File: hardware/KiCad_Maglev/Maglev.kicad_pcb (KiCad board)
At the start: 4 copper layers, 265 x 130 mm, 97 parts, among them IC1 TLV1117LV33DCYR, J1 USB_C_Receptacle, J2 691103110002, J3 61300621121, J4 61300821121, J5 61300821121, J6 61300621121, U1 WE-TVS-82400102, U2 ESP32-C3, U4 TMAG5173A2QDBVRQ1, U5 TPS259474ARPWR, Y1 IQXC-42_830108213209

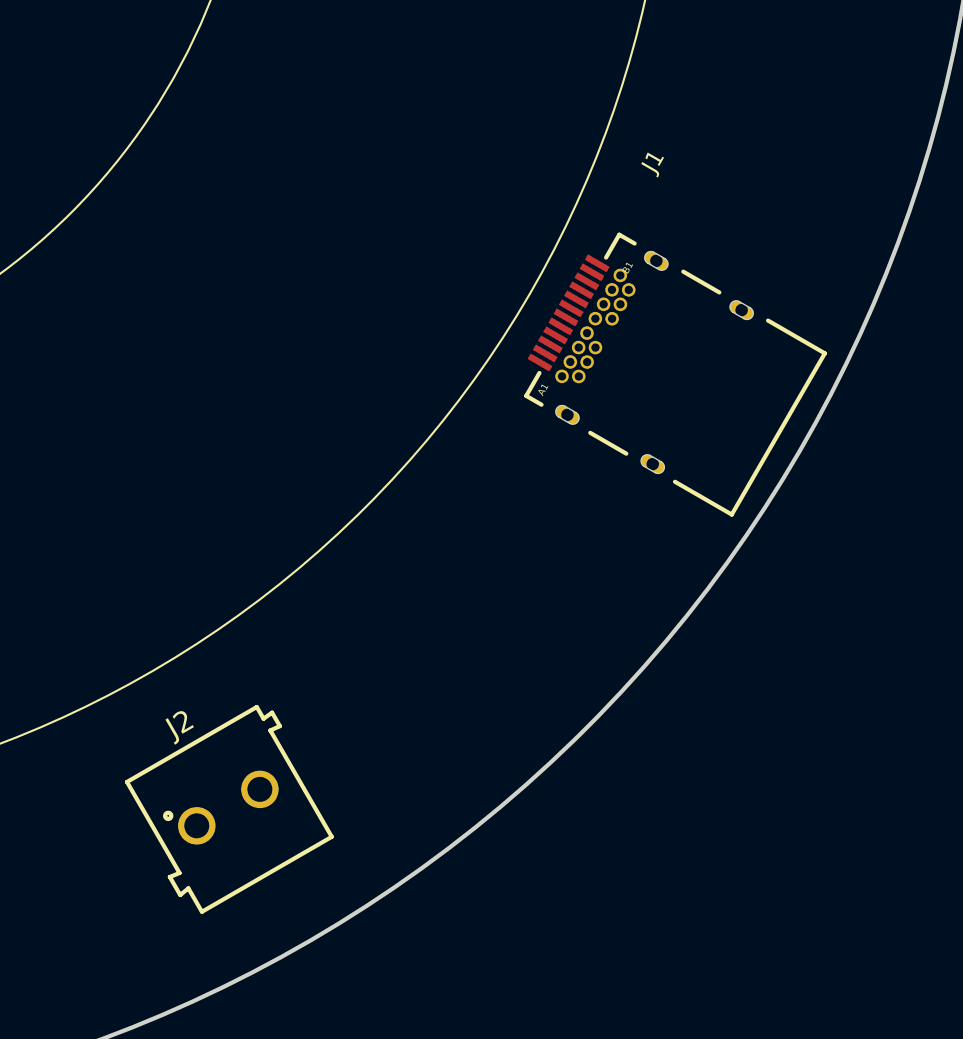
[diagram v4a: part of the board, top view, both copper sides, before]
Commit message: changed usb connector from 30deg to 45deg for easier routing
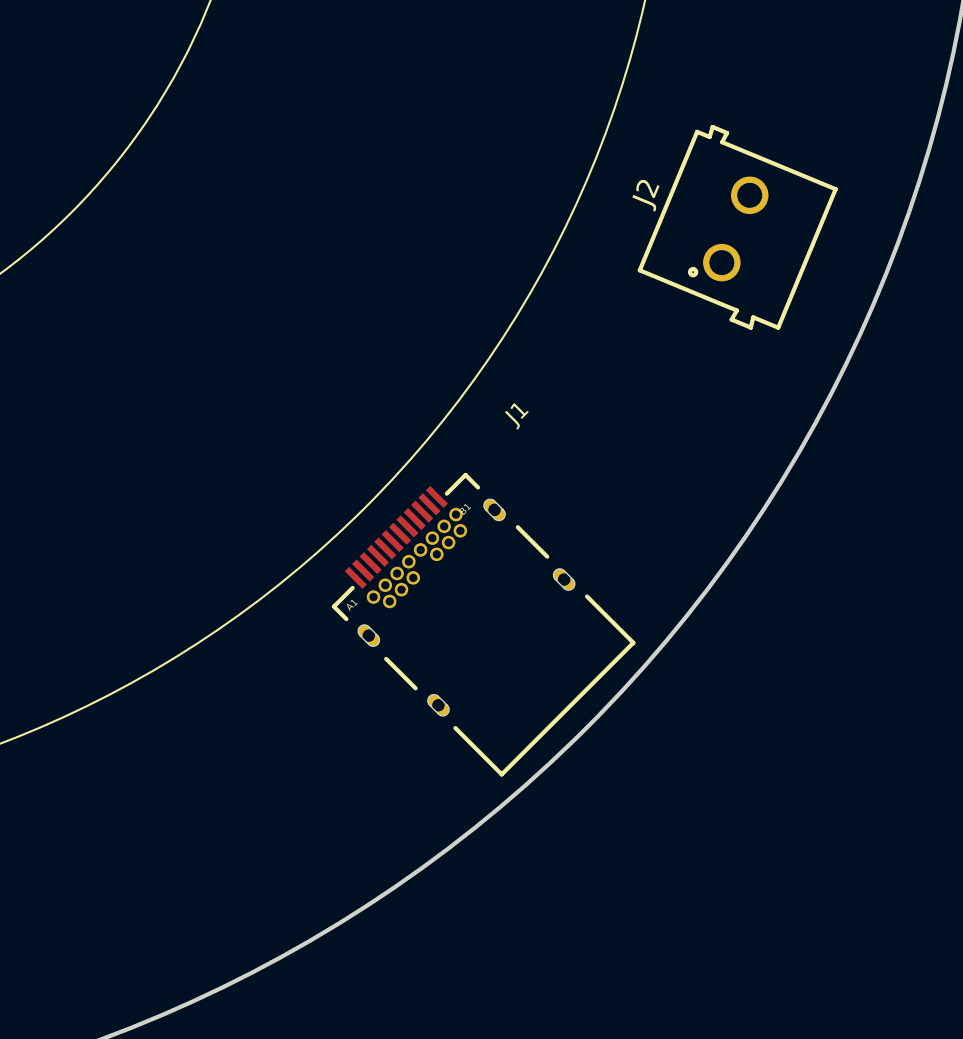
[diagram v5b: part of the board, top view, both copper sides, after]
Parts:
- moved J2 37.0 mm to (268.1, 122.0), turned to 67.5 degrees
- moved J1 15.1 mm to (256.0, 141.0), turned to 45 degrees

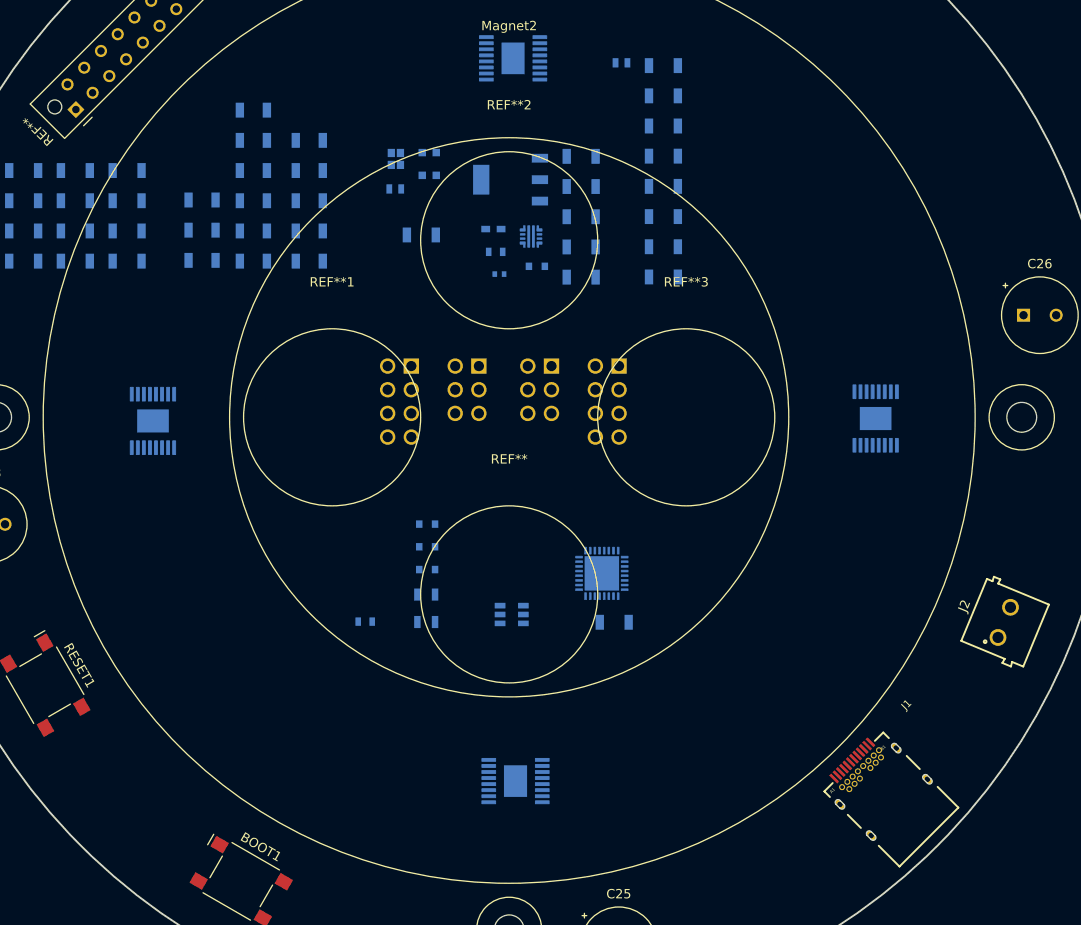
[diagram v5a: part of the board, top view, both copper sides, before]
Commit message: added hex nuts for 15mm spacers on controller pcb
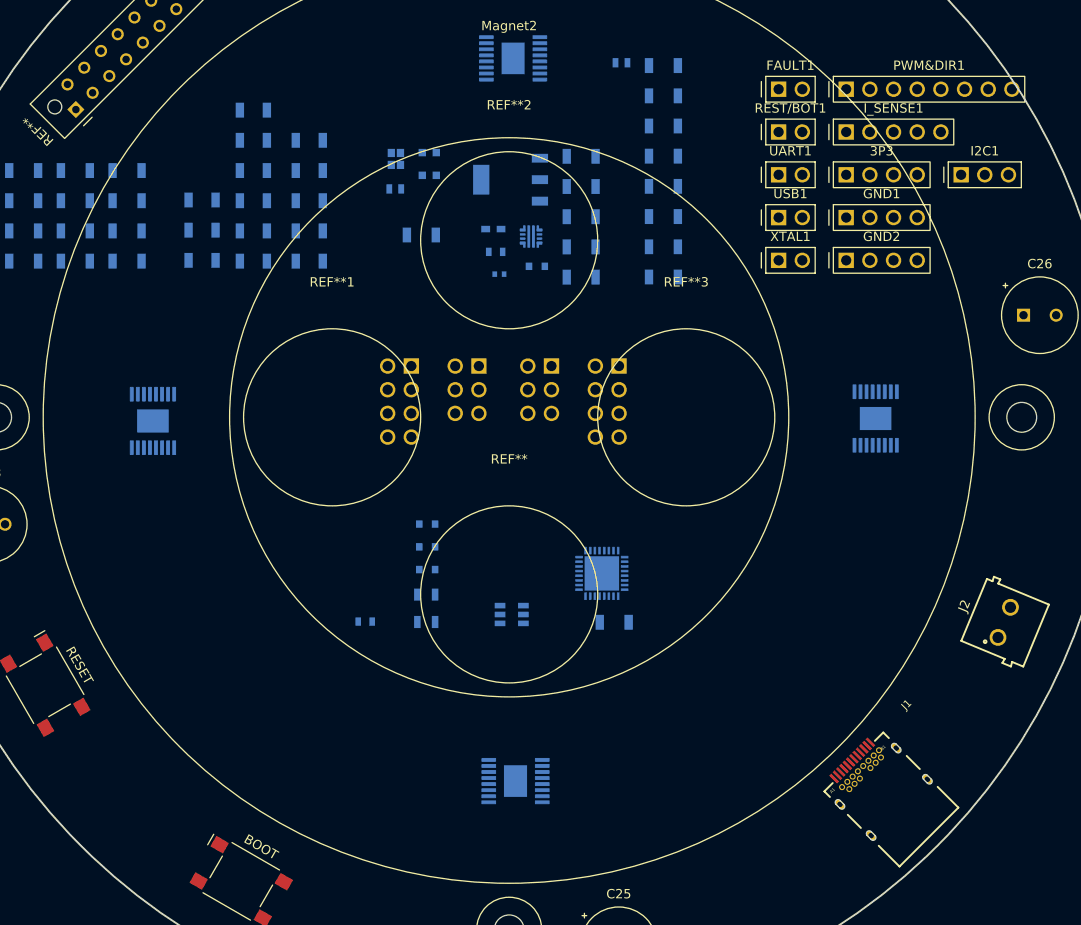
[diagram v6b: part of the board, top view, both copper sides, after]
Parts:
- added 3P3: 61300411121, Connector_THT_Wurth:J_Wurth_WR-PHD_61300411121, F.Cu at (251.2, 74.0)
- added FAULT1: 61300211121, Connector_THT_Wurth:J_Wurth_WR-PHD_61300211121, F.Cu at (243.9, 64.8)
- added GND1: 61300411121, Connector_THT_Wurth:J_Wurth_WR-PHD_61300411121, F.Cu at (251.2, 78.6)
- added GND2: 61300411121, Connector_THT_Wurth:J_Wurth_WR-PHD_61300411121, F.Cu at (251.2, 83.2)
- added I2C1: 61300311121, Connector_THT_Wurth:J_Wurth_WR-PHD_61300311121, F.Cu at (263.5, 74.0)
- added I_SENSE1: 61300511121, Connector_THT_Wurth:J_Wurth_WR-PHD_61300511121, F.Cu at (251.2, 69.4)
- added PWM&DIR1: 61300811121, Connector_THT_Wurth:J_Wurth_WR-PHD_61300811121, F.Cu at (251.2, 64.8)
- added REST/BOT1: 61300211121, Connector_THT_Wurth:J_Wurth_WR-PHD_61300211121, F.Cu at (243.9, 69.4)
- added UART1: 61300211121, Connector_THT_Wurth:J_Wurth_WR-PHD_61300211121, F.Cu at (243.9, 74.0)
- added USB1: 61300211121, Connector_THT_Wurth:J_Wurth_WR-PHD_61300211121, F.Cu at (243.9, 78.6)
- added XTAL1: 61300211121, Connector_THT_Wurth:J_Wurth_WR-PHD_61300211121, F.Cu at (243.9, 83.2)
- renumbered BOOT1 to BOOT, RESET1 to RESET

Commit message: Route power PCB and implement board-to-board connector
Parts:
- removed the REF** at (168.5, 67.0)
- removed the REF** at (47.0, 53.5)
- added J11: 690367190672, Connector_THT_Wurth:J_Wurth_WR-MM_690367190672, F.Cu at (252.5, 58.0)
- added J12: 690367190672, Connector_THT_Wurth:J_Wurth_WR-MM_690367190672, B.Cu at (119.3, 56.2)
- added J7: 690367191672, Connector_THT_Wurth:J_Wurth_WR-MM_690367191672, F.Cu at (180.2, 51.7)
- added J8: 690367191672, Connector_THT_Wurth:J_Wurth_WR-MM_690367191672, B.Cu at (47.0, 53.5)
- POWER_LED2: moved to F.Cu
- moved C10 159.0 mm to (362.4, 54.2)
- moved C11 159.0 mm to (330.9, 47.3)
- moved C12 159.0 mm to (330.9, 50.5)
- moved C13 159.0 mm to (330.9, 53.8)
- moved C14 159.0 mm to (330.9, 57.0)
- moved C15 159.0 mm to (325.3, 47.3)
- moved C16 159.0 mm to (325.3, 50.5)
- moved C19 159.0 mm to (325.3, 53.8)
- moved C20 159.0 mm to (325.3, 57.0)
- moved I2C1 159.0 mm to (420.3, 47.7)
- moved J5 159.0 mm to (361.4, 68.3)
- moved J6 159.0 mm to (368.6, 68.3)
- moved POWER_LED1 159.0 mm to (363.1, 85.2)
- moved Status_LED_RX1 159.0 mm to (363.1, 87.7)
- moved Status_LED_TX1 159.0 mm to (363.1, 90.1)
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- renumbered BOOT to BOOT1, RESET to RESET1
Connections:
- net /Electromagnet Driver/EM_A_N renamed /EM_A_N
- net /Electromagnet Driver/EM_A_P renamed /EM_A_P
- net /Electromagnet Driver/EM_B_N renamed /EM_B_N
- net /Electromagnet Driver/EM_B_P renamed /EM_B_P
- net /Electromagnet Driver/EM_C_N renamed /EM_C_N
- net /Electromagnet Driver/EM_C_P renamed /EM_C_P
- net /Electromagnet Driver/EM_D_N renamed /EM_D_N
- net /Electromagnet Driver/EM_D_P renamed /EM_D_P
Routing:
- net /EM_D_P: track 0.00 -> 110.0 mm
- net /EM_D_N: track 0.00 -> 93.4 mm
- net /EM_C_P: track 0.00 -> 82.1 mm
- net /EM_C_N: track 0.00 -> 71.3 mm
- net /EM_B_P: track 0.00 -> 61.7 mm
- net /I2C_SCL: track 0.00 -> 60.2 mm
- net /I2C_INT: track 0.00 -> 58.8 mm
- net /I2C_SDA: track 0.00 -> 58.1 mm
- net /EM_A_N: track 0.00 -> 56.0 mm
- net /EM_B_N: track 0.00 -> 55.9 mm
- net /EM_A_P: track 0.00 -> 55.4 mm
- net GND: track 0.00 -> 24.9 mm, vias 0 -> 11
- net +3.3V: track 0.00 -> 4.62 mm, vias 0 -> 2
- net Net-(U5-DVDT): track 0.00 -> 1.70 mm
- added copper zone on In2.Cu, net +3.3V
- added copper zone on In1.Cu, net GND

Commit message: Update Rooting ESP32
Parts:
- 3P3, FAULT1, GND1, GND2, I_SENSE1, PWM&DIR1, REST/BOT1, USB1, XTAL1: moved to B.Cu
- C1, POWER_LED1: moved to F.Cu
- moved C10 287.1 mm to (79.5, 103.0)
- moved R8 256.5 mm to (90.5, 114.5), turned to 90 degrees
- moved R10 252.1 mm to (93.5, 114.5), turned to 90 degrees
- moved R9 249.4 mm to (97.0, 114.5), turned to 90 degrees
- moved C1 218.0 mm to (168.5, 134.0), turned to -150 degrees
- moved R3 198.0 mm to (173.5, 133.0), turned to 90 degrees
- moved R4 185.7 mm to (197.0, 152.0)
- moved R5 185.3 mm to (197.0, 154.5)
- moved C3 184.1 mm to (223.0, 120.0), turned to -90 degrees
- moved C2 183.1 mm to (227.5, 123.5), turned to -90 degrees
- moved C5 182.9 mm to (217.5, 111.0)
- moved POWER_LED1 182.7 mm to (193.0, 152.0), turned to -120 degrees
- moved C4 180.9 mm to (220.0, 108.5), turned to 135 degrees
- moved C8 180.4 mm to (217.6, 113.5)
- moved L5 180.0 mm to (223.0, 116.5)
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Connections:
- U1 pad 3: /+USB_D -> /USB_D+
- U1 pad 4: /-USB_D -> /USB_D-
- U2 pad 25: /+USB_D -> /USB_D+
- U2 pad 26: /-USB_D -> /USB_D-
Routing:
- net +V_HB: track 0.00 -> 425.3 mm, vias 0 -> 2
- net GND: track 24.9 -> 147.1 mm, vias 11 -> 61
- net /I2C_SCL: track 60.2 -> 165.4 mm, vias 0 -> 2
- net /I2C_SDA: track 58.1 -> 161.7 mm, vias 0 -> 2
- net /EM_C_N: track 71.3 -> 172.5 mm, vias 0 -> 1
- net /EM_B_N: track 55.9 -> 154.2 mm, vias 0 -> 1
- net /I2C_INT: track 58.8 -> 156.8 mm, vias 0 -> 2
- net /EM_B_P: track 61.7 -> 157.4 mm, vias 0 -> 1
- net /EM_C_P: track 82.1 -> 176.9 mm, vias 0 -> 1
- net /BOOT: track 0.00 -> 76.8 mm, vias 0 -> 2
- net /CHIP_EN: track 0.00 -> 72.2 mm, vias 0 -> 1
- net +3.3V: track 4.62 -> 71.7 mm, vias 2 -> 20
- net +5VP: track 0.20 -> 56.3 mm, vias 0 -> 1
- net /EM_D_N: track 93.4 -> 147.2 mm, vias 0 -> 1
- net /EM_A_P: track 55.4 -> 100.4 mm, vias 0 -> 1
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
